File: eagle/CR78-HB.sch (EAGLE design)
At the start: 35 parts, among them Q1 2N3904, Q2 2N3904, Q3 2N3904, X1 22-23-2021

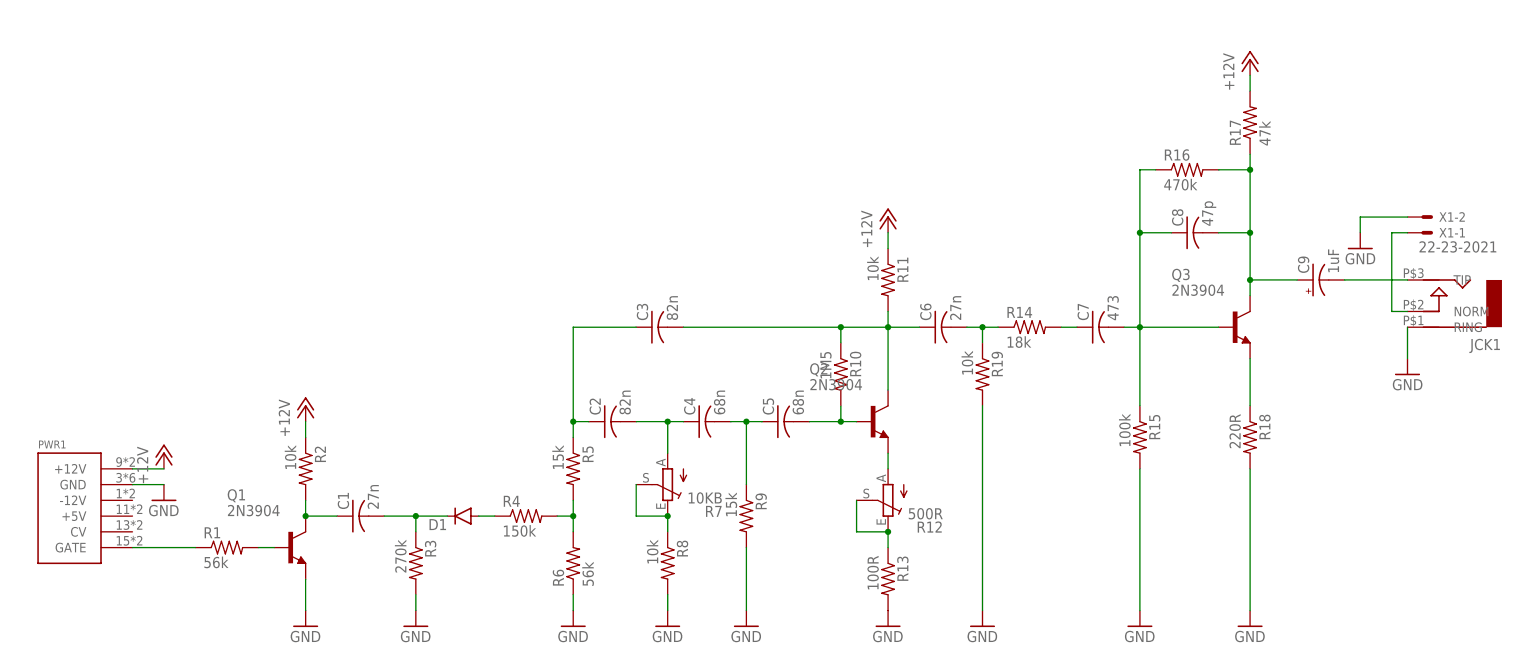
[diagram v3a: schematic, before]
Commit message: routed with panel pots
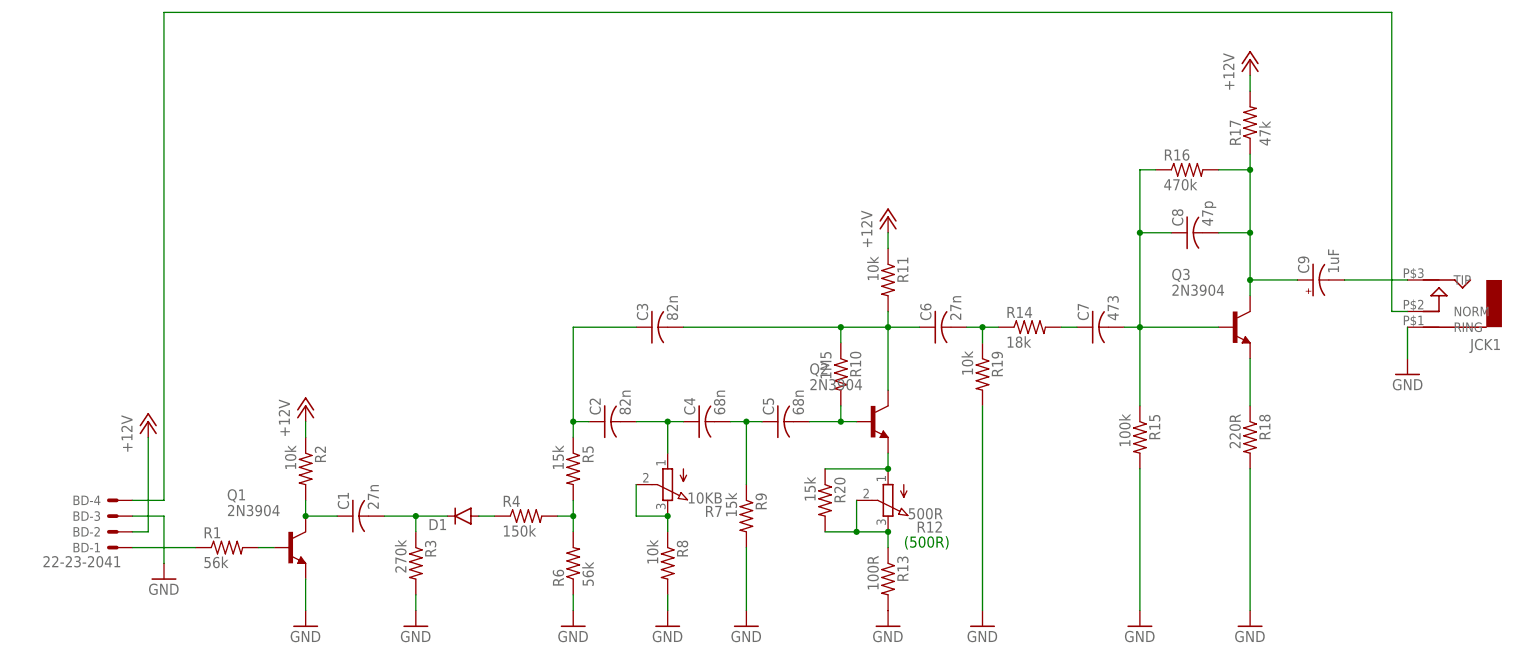
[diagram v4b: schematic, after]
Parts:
- removed PWR1: POWER, eurorack:POWER
- removed X1: 22-23-2021, con-molex:22-23-2021
- added BD: 22-23-2041, con-molex:22-23-2041
- added R20: 15k, rcl:R-US_0207/5V
- R12, R7: device TR808clone:TRIM_EU-B64Y -> pot:3RP/1610N
- R18: device rcl:R-US_0207/2V -> rcl:R-US_0207/7
- R19: device rcl:R-US_0207/2V -> rcl:R-US_0207/5V
- R9: device rcl:R-US_0207/7 -> rcl:R-US_0207/5V
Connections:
- net +12V: now also BD-2.S; no longer PWR1.+12V
- net GND: now also BD-3.S; no longer PWR1.GND, X1-2.S
- net N$11: now also BD-1.S; no longer PWR1.GATE
- net N$12: now also BD-4.S; no longer X1-1.S
- net N$13: now also R20.1
- net N$8: now also R20.2
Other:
- note added: "(500R)"
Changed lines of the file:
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@@
 <?xml version="1.0" encoding="utf-8"?>
 <!DOCTYPE eagle SYSTEM "eagle.dtd">
-<eagle version="7.2.0">
+<eagle version="7.6.0">
 <drawing>
 <settings>
@@
 <part name="R2" library="rcl" deviceset="R-US_" device="0207/7" value="10k"/>
 <part name="R1" library="rcl" deviceset="R-US_" device="0207/7" value="56k"/>
-<part name="PWR1" library="eurorack" deviceset="POWER" device=""/>
 <part name="P+1" library="supply1" deviceset="+12V" device=""/>
 <part name="GND1" library="supply1" deviceset="GND" device=""/>
@@
 <part name="C4" library="rcl" deviceset="C-US" device="050-025X075" value="68n"/>
 <part name="R8" library="rcl" deviceset="R-US_" device="0207/7" value="10k"/>
-<part name="R7" library="TR808clone" deviceset="TRIM_EU-" device="B64Y" value="10KB"/>
+<part name="R7" library="pot" deviceset="3RP/1610N" device="" value="10KB"/>
 <part name="C5" library="rcl" deviceset="C-US" device="050-025X075" value="68n"/>
-<part name="R9" library="rcl" deviceset="R-US_" device="0207/7" value="15k"/>
+<part name="R9" library="rcl" deviceset="R-US_" device="0207/5V" value="15k"/>
 <part name="Q2" library="808_lt" deviceset="2N3904" device=""/>
 <part name="R13" library="rcl" deviceset="R-US_" device="0207/7" value="100R"/>
@@
 <part name="R14" library="rcl" deviceset="R-US_" device="0207/7" value="18k"/>
 <part name="C6" library="rcl" deviceset="C-US" device="050-025X075" value="27n"/>
-<part name="R12" library="TR808clone" deviceset="TRIM_EU-" device="B64Y" value="500R"/>
+<part name="R12" library="pot" deviceset="3RP/1610N" device="" value="500R"/>
 <part name="GND4" library="supply1" deviceset="GND" device=""/>
 <part name="GND5" library="supply1" deviceset="GND" device=""/>
@@
 <part name="R16" library="rcl" deviceset="R-US_" device="0207/7" value="470k"/>
 <part name="R17" library="rcl" deviceset="R-US_" device="0207/7" value="47k"/>
-<part name="R18" library="rcl" deviceset="R-US_" device="0207/2V" value="220R"/>
+<part name="R18" library="rcl" deviceset="R-US_" device="0207/7" value="220R"/>
 <part name="C9" library="rcl" deviceset="CPOL-US" device="B45181A" value="1uF"/>
 <part name="JCK1" library="erthenvar" deviceset="AUDIO-JACK" device=""/>
-<part name="X1" library="con-molex" deviceset="22-23-2021" device=""/>
-<part name="GND10" library="supply1" deviceset="GND" device=""/>
 <part name="GND11" library="supply1" deviceset="GND" device=""/>
 <part name="P+4" library="supply1" deviceset="+12V" device=""/>
@@
 <part name="R15" library="rcl" deviceset="R-US_" device="0207/7" value="100k"/>
 <part name="GND8" library="supply1" deviceset="GND" device=""/>
-<part name="R19" library="rcl" deviceset="R-US_" device="0207/2V" value="10k"/>
+<part name="R19" library="rcl" deviceset="R-US_" device="0207/5V" value="10k"/>
 <part name="GND12" library="supply1" deviceset="GND" device=""/>
+<part name="BD" library="con-molex" deviceset="22-23-2041" device=""/>
+<part name="R20" library="rcl" deviceset="R-US_" device="0207/5V" value="15k"/>
 </parts>
 <sheets>
 <sheet>
 <plain>
+<text x="121.92" y="43.18" size="1.778" layer="91">(500R)</text>
 </plain>
 <instances>
@@
 <instance part="R2" gate="G$1" x="25.4" y="55.88" rot="R270"/>
 <instance part="R1" gate="G$1" x="12.7" y="43.18"/>
-<instance part="PWR1" gate="G$1" x="-12.7" y="50.8"/>
-<instance part="P+1" gate="1" x="2.54" y="58.42"/>
-<instance part="GND1" gate="1" x="2.54" y="50.8"/>
+<instance part="P+1" gate="1" x="0" y="63.5"/>
+<instance part="GND1" gate="1" x="2.54" y="38.1"/>
 <instance part="C1" gate="G$1" x="33.02" y="48.26" rot="R90"/>
 <instance part="R3" gate="G$1" x="43.18" y="40.64" rot="R270"/>
@@
 <instance part="C4" gate="G$1" x="88.9" y="63.5" rot="R90"/>
 <instance part="R8" gate="G$1" x="83.82" y="40.64" rot="R270"/>
-<instance part="R7" gate="1" x="83.82" y="53.34" smashed="yes" rot="R180">
+<instance part="R7" gate="G$1" x="83.82" y="53.34" smashed="yes" rot="R180">
 <attribute name="NAME" x="92.71" y="49.911" size="1.778" layer="95" rot="R180"/>
 <attribute name="VALUE" x="92.71" y="52.07" size="1.778" layer="96" rot="R180"/>
@@
 <instance part="R14" gate="G$1" x="142.24" y="78.74"/>
 <instance part="C6" gate="G$1" x="127" y="78.74" rot="R90"/>
-<instance part="R12" gate="1" x="119.38" y="50.8" smashed="yes" rot="R180">
+<instance part="R12" gate="G$1" x="119.38" y="50.8" smashed="yes" rot="R180">
 <attribute name="NAME" x="128.27" y="47.371" size="1.778" layer="95" rot="R180"/>
 <attribute name="VALUE" x="128.27" y="49.53" size="1.778" layer="96" rot="R180"/>
@@
 <instance part="C9" gate="G$1" x="187.96" y="86.36" rot="R90"/>
 <instance part="JCK1" gate="G$1" x="210.82" y="81.28" rot="R180"/>
-<instance part="X1" gate="-1" x="205.74" y="93.98" rot="MR180"/>
-<instance part="X1" gate="-2" x="205.74" y="96.52" rot="MR180"/>
-<instance part="GND10" gate="1" x="195.58" y="91.44" rot="MR0"/>
 <instance part="GND11" gate="1" x="203.2" y="71.12" rot="MR0"/>
 <instance part="P+4" gate="1" x="177.8" y="121.92"/>
@@
 <instance part="R19" gate="G$1" x="134.62" y="71.12" rot="R270"/>
 <instance part="GND12" gate="1" x="134.62" y="30.48"/>
+<instance part="BD" gate="-1" x="-5.08" y="43.18" rot="R180"/>
+<instance part="BD" gate="-2" x="-5.08" y="45.72" rot="R180"/>
+<instance part="BD" gate="-3" x="-5.08" y="48.26" rot="R180"/>
+<instance part="BD" gate="-4" x="-5.08" y="50.8" rot="R180"/>
+<instance part="R20" gate="G$1" x="109.22" y="50.8" rot="R270"/>
 </instances>
 <busses>
@@
 </segment>
 <segment>
-<pinref part="PWR1" gate="G$1" pin="+12V"/>
-<wire x1="-2.54" y1="55.88" x2="2.54" y2="55.88" width="0.1524" layer="91"/>
+<wire x1="-2.54" y1="45.72" x2="0" y2="45.72" width="0.1524" layer="91"/>
+<wire x1="0" y1="45.72" x2="0" y2="60.96" width="0.1524" layer="91"/>
 <pinref part="P+1" gate="1" pin="+12V"/>
+<pinref part="BD" gate="-2" pin="S"/>
 </segment>
 <segment>
@@
 </segment>
 <segment>
-<pinref part="PWR1" gate="G$1" pin="GND"/>
-<wire x1="-2.54" y1="53.34" x2="2.54" y2="53.34" width="0.1524" layer="91"/>
+<wire x1="-2.54" y1="48.26" x2="2.54" y2="48.26" width="0.1524" layer="91"/>
+<wire x1="2.54" y1="48.26" x2="2.54" y2="40.64" width="0.1524" layer="91"/>
 <pinref part="GND1" gate="1" pin="GND"/>
+<pinref part="BD" gate="-3" pin="S"/>
 </segment>
 <segment>
@@
 <pinref part="R13" gate="G$1" pin="2"/>
 <pinref part="GND7" gate="1" pin="GND"/>
-</segment>
-<segment>
-<pinref part="X1" gate="-2" pin="S"/>
-<wire x1="203.2" y1="96.52" x2="195.58" y2="96.52" width="0.1524" layer="91"/>
-<wire x1="195.58" y1="96.52" x2="195.58" y2="93.98" width="0.1524" layer="91"/>
-<pinref part="GND10" gate="1" pin="GND"/>
 </segment>
 <segment>
@@
 <net name="N$5" class="0">
 <segment>
-<pinref part="R7" gate="1" pin="E"/>
-<pinref part="R7" gate="1" pin="S"/>
+<pinref part="R7" gate="G$1" pin="E"/>
+<pinref part="R7" gate="G$1" pin="S"/>
 <wire x1="83.82" y1="48.26" x2="78.74" y2="48.26" width="0.1524" layer="91"/>
 <wire x1="78.74" y1="48.26" x2="78.74" y2="53.34" width="0.1524" layer="91"/>
@@
 <net name="N$6" class="0">
 <segment>
-<pinref part="R7" gate="1" pin="A"/>
+<pinref part="R7" gate="G$1" pin="A"/>
 <wire x1="83.82" y1="58.42" x2="83.82" y2="63.5" width="0.1524" layer="91"/>
 <pinref part="C2" gate="G$1" pin="2"/>
@@
 <net name="N$8" class="0">
 <segment>
-<pinref part="R12" gate="1" pin="E"/>
+<pinref part="R12" gate="G$1" pin="E"/>
 <pinref part="R13" gate="G$1" pin="1"/>
 <wire x1="119.38" y1="43.18" x2="119.38" y2="45.72" width="0.1524" layer="91"/>
-<pinref part="R12" gate="1" pin="S"/>
+<pinref part="R12" gate="G$1" pin="S"/>
 <wire x1="114.3" y1="50.8" x2="114.3" y2="45.72" width="0.1524" layer="91"/>
 <wire x1="114.3" y1="45.72" x2="119.38" y2="45.72" width="0.1524" layer="91"/>
 <junction x="119.38" y="45.72"/>
+<pinref part="R20" gate="G$1" pin="2"/>
+<wire x1="109.22" y1="45.72" x2="114.3" y2="45.72" width="0.1524" layer="91"/>
+<junction x="114.3" y="45.72"/>
 </segment>
 </net>
@@
 <segment>
 <pinref part="R1" gate="G$1" pin="1"/>
-<pinref part="PWR1" gate="G$1" pin="GATE"/>
 <wire x1="-2.54" y1="43.18" x2="7.62" y2="43.18" width="0.1524" layer="91"/>
+<pinref part="BD" gate="-1" pin="S"/>
 </segment>
 </net>
 <net name="N$13" class="0">
 <segment>
-<pinref part="R12" gate="1" pin="A"/>
+<pinref part="R12" gate="G$1" pin="A"/>
 <pinref part="Q2" gate="G1" pin="E"/>
 <wire x1="119.38" y1="55.88" x2="119.38" y2="58.42" width="0.1524" layer="91"/>
+<pinref part="R20" gate="G$1" pin="1"/>
+<wire x1="109.22" y1="55.88" x2="119.38" y2="55.88" width="0.1524" layer="91"/>
+<junction x="119.38" y="55.88"/>
 </segment>
 </net>
@@
 <pinref part="JCK1" gate="G$1" pin="NORM"/>
 <wire x1="203.2" y1="81.28" x2="200.66" y2="81.28" width="0.1524" layer="91"/>
-<wire x1="200.66" y1="81.28" x2="200.66" y2="93.98" width="0.1524" layer="91"/>
-<pinref part="X1" gate="-1" pin="S"/>
-<wire x1="200.66" y1="93.98" x2="203.2" y2="93.98" width="0.1524" layer="91"/>
-</segment>
-</net>
+<wire x1="200.66" y1="81.28" x2="200.66" y2="129.54" width="0.1524" layer="91"/>
+<wire x1="200.66" y1="129.54" x2="2.54" y2="129.54" width="0.1524" layer="91"/>
+<wire x1="2.54" y1="129.54" x2="2.54" y2="50.8" width="0.1524" layer="91"/>
+<pinref part="BD" gate="-4" pin="S"/>
+<wire x1="2.54" y1="50.8" x2="-2.54" y2="50.8" width="0.1524" layer="91"/>
+</segment>
+</net>

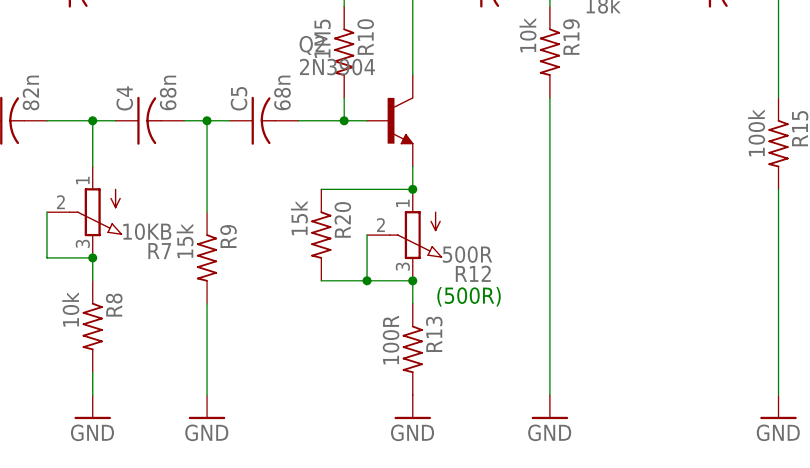
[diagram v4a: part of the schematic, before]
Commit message: routed with pot change resistor value
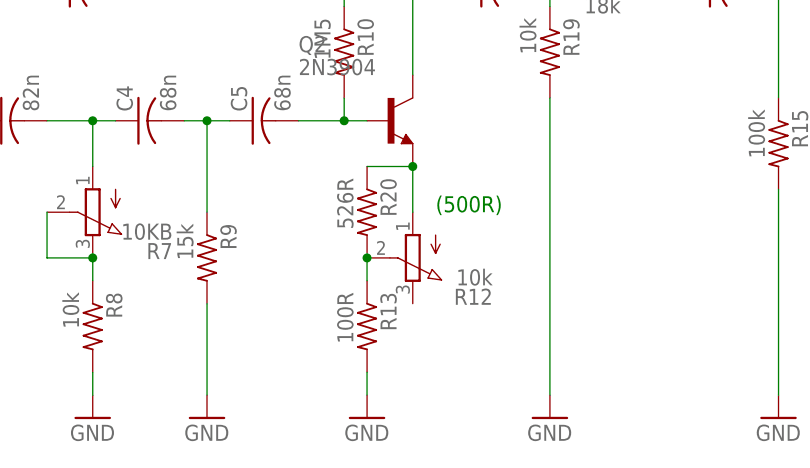
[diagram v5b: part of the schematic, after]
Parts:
- R12: value 500R -> 10k
- R20: value 15k -> 526R
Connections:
- net N$8: no longer R12.E
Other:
- moved on the sheet: R12, R13, R20
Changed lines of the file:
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@@
 <part name="R14" library="rcl" deviceset="R-US_" device="0207/7" value="18k"/>
 <part name="C6" library="rcl" deviceset="C-US" device="050-025X075" value="27n"/>
-<part name="R12" library="pot" deviceset="3RP/1610N" device="" value="500R"/>
+<part name="R12" library="pot" deviceset="3RP/1610N" device="" value="10k"/>
 <part name="GND4" library="supply1" deviceset="GND" device=""/>
 <part name="GND5" library="supply1" deviceset="GND" device=""/>
@@
 <part name="GND12" library="supply1" deviceset="GND" device=""/>
 <part name="BD" library="con-molex" deviceset="22-23-2041" device=""/>
-<part name="R20" library="rcl" deviceset="R-US_" device="0207/5V" value="15k"/>
+<part name="R20" library="rcl" deviceset="R-US_" device="0207/5V" value="526R"/>
 </parts>
 <sheets>
 <sheet>
 <plain>
-<text x="121.92" y="43.18" size="1.778" layer="91">(500R)</text>
+<text x="121.92" y="53.34" size="1.778" layer="91">(500R)</text>
 </plain>
 <instances>
@@
 <instance part="R9" gate="G$1" x="96.52" y="48.26" rot="R270"/>
 <instance part="Q2" gate="G1" x="116.84" y="63.5"/>
-<instance part="R13" gate="G$1" x="119.38" y="38.1" rot="R270"/>
+<instance part="R13" gate="G$1" x="114.3" y="40.64" rot="R270"/>
 <instance part="R10" gate="G$1" x="111.76" y="71.12" rot="R270"/>
 <instance part="R11" gate="G$1" x="119.38" y="86.36" rot="R270"/>
 <instance part="R14" gate="G$1" x="142.24" y="78.74"/>
 <instance part="C6" gate="G$1" x="127" y="78.74" rot="R90"/>
-<instance part="R12" gate="G$1" x="119.38" y="50.8" smashed="yes" rot="R180">
-<attribute name="NAME" x="128.27" y="47.371" size="1.778" layer="95" rot="R180"/>
-<attribute name="VALUE" x="128.27" y="49.53" size="1.778" layer="96" rot="R180"/>
+<instance part="R12" gate="G$1" x="119.38" y="48.26" smashed="yes" rot="R180">
+<attribute name="NAME" x="128.27" y="44.831" size="1.778" layer="95" rot="R180"/>
+<attribute name="VALUE" x="128.27" y="46.99" size="1.778" layer="96" rot="R180"/>
 </instance>
 <instance part="GND4" gate="1" x="68.58" y="30.48"/>
 <instance part="GND5" gate="1" x="83.82" y="30.48"/>
 <instance part="GND6" gate="1" x="96.52" y="30.48"/>
-<instance part="GND7" gate="1" x="119.38" y="30.48"/>
+<instance part="GND7" gate="1" x="114.3" y="30.48"/>
 <instance part="P+3" gate="1" x="119.38" y="96.52"/>
 <instance part="C7" gate="G$1" x="152.4" y="78.74" rot="R90"/>
@@
 <instance part="BD" gate="-3" x="-5.08" y="48.26" rot="R180"/>
 <instance part="BD" gate="-4" x="-5.08" y="50.8" rot="R180"/>
-<instance part="R20" gate="G$1" x="109.22" y="50.8" rot="R270"/>
+<instance part="R20" gate="G$1" x="114.3" y="53.34" rot="R270"/>
 </instances>
 <busses>
@@
 <pinref part="R13" gate="G$1" pin="2"/>
 <pinref part="GND7" gate="1" pin="GND"/>
+<wire x1="114.3" y1="35.56" x2="114.3" y2="33.02" width="0.1524" layer="91"/>
 </segment>
 <segment>
@@
 <net name="N$8" class="0">
 <segment>
-<pinref part="R12" gate="G$1" pin="E"/>
+<pinref part="R12" gate="G$1" pin="S"/>
+<pinref part="R20" gate="G$1" pin="2"/>
+<junction x="114.3" y="48.26"/>
 <pinref part="R13" gate="G$1" pin="1"/>
-<wire x1="119.38" y1="43.18" x2="119.38" y2="45.72" width="0.1524" layer="91"/>
-<pinref part="R12" gate="G$1" pin="S"/>
-<wire x1="114.3" y1="50.8" x2="114.3" y2="45.72" width="0.1524" layer="91"/>
-<wire x1="114.3" y1="45.72" x2="119.38" y2="45.72" width="0.1524" layer="91"/>
-<junction x="119.38" y="45.72"/>
-<pinref part="R20" gate="G$1" pin="2"/>
-<wire x1="109.22" y1="45.72" x2="114.3" y2="45.72" width="0.1524" layer="91"/>
-<junction x="114.3" y="45.72"/>
+<wire x1="114.3" y1="45.72" x2="114.3" y2="48.26" width="0.1524" layer="91"/>
 </segment>
 </net>
@@
 <pinref part="R12" gate="G$1" pin="A"/>
 <pinref part="Q2" gate="G1" pin="E"/>
-<wire x1="119.38" y1="55.88" x2="119.38" y2="58.42" width="0.1524" layer="91"/>
+<wire x1="119.38" y1="53.34" x2="119.38" y2="58.42" width="0.1524" layer="91"/>
 <pinref part="R20" gate="G$1" pin="1"/>
-<wire x1="109.22" y1="55.88" x2="119.38" y2="55.88" width="0.1524" layer="91"/>
-<junction x="119.38" y="55.88"/>
-</segment>
-</net>
+<wire x1="114.3" y1="58.42" x2="119.38" y2="58.42" width="0.1524" layer="91"/>
+<junction x="119.38" y="58.42"/>
+</segment>
+</net>
